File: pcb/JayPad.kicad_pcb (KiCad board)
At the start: 2 copper layers, 113 x 70.8 mm, 51 parts, among them M1 MOUDLE-SEEEDUINO-XIAO, SW1 PEC11-4215F-S24

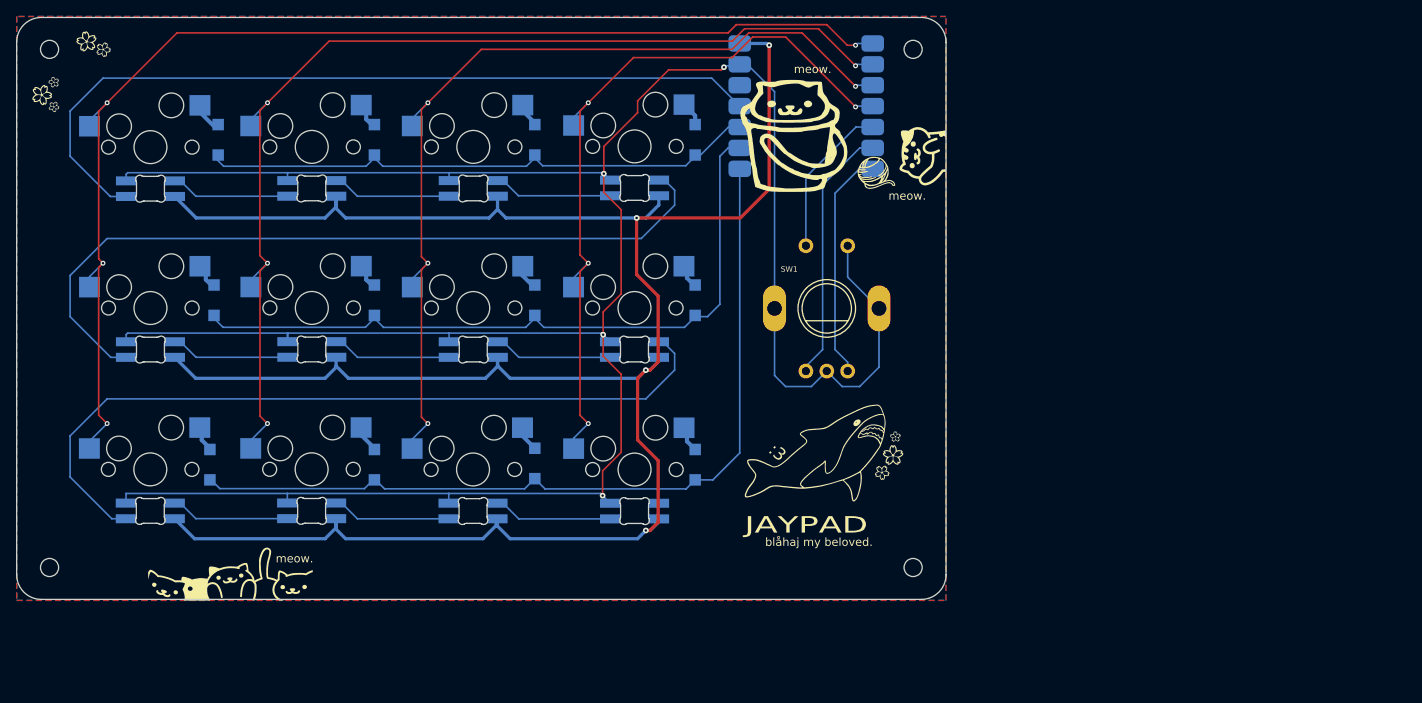
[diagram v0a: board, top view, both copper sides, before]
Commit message: LEDs now using GND copper pour & routed ROW0 which I somehow forgot to do
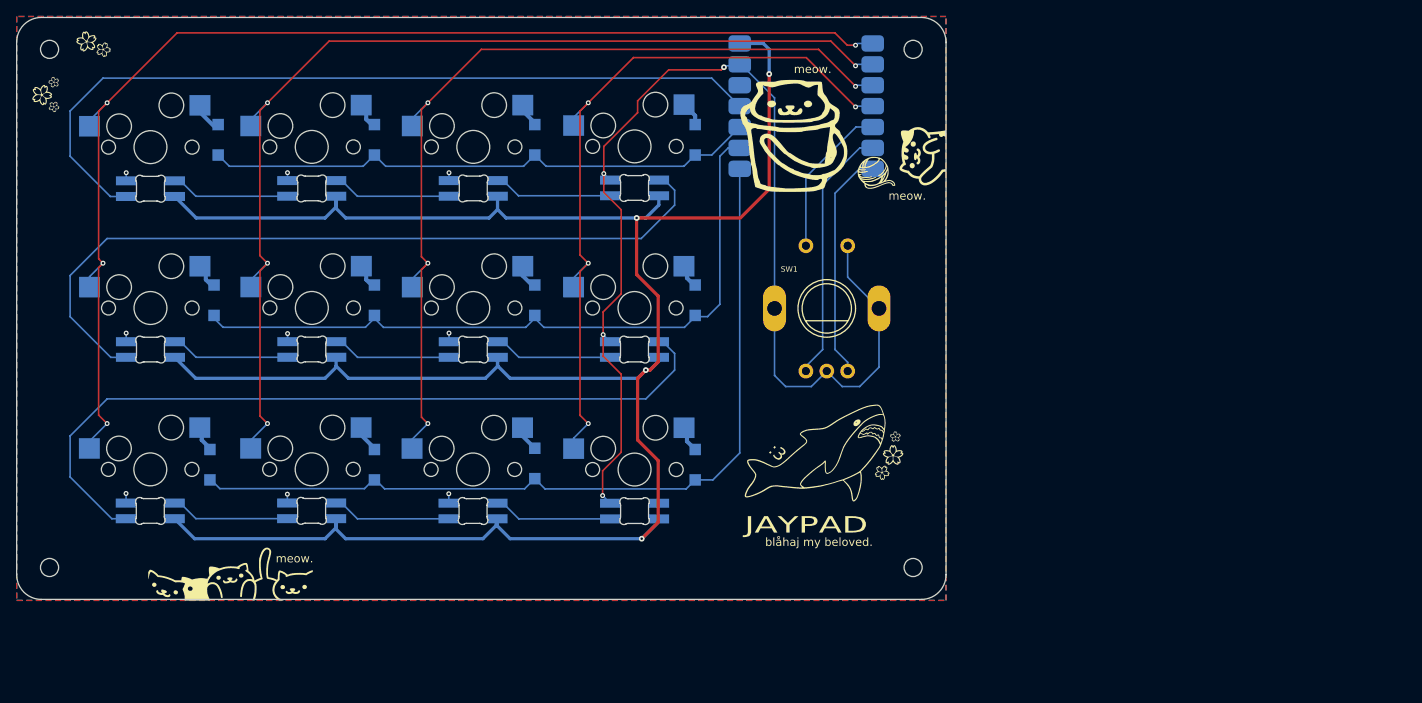
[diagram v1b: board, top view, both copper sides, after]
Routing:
- net GND: track 327.7 -> 152.3 mm, vias 4 -> 13
- net COL3: track 92.9 -> 90.8 mm
- net COL2: track 111.6 -> 109.9 mm
- net COL1: track 130.8 -> 129.5 mm
- net +5V: track 283.9 -> 284.9 mm
- net COL0: track 149.4 -> 148.6 mm

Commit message: Changed from RGB backlight to underglow
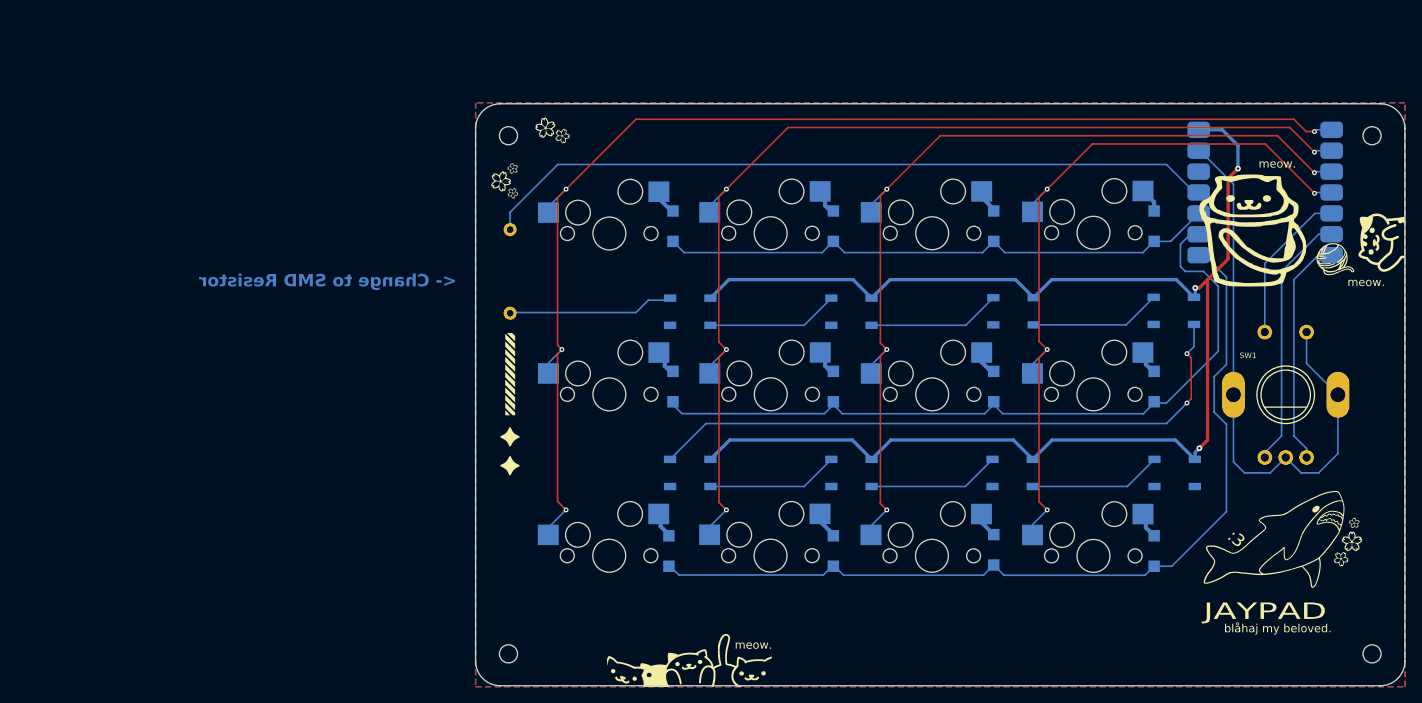
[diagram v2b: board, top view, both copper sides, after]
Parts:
- added G***: LOGO, LOGO, F.Cu at (95.0, 102.5)
- added G***: LOGO, LOGO, F.Cu at (95.0, 91.5)
- added G***: LOGO, LOGO, F.Cu at (95.0, 99.0)
- added LED1: WS2812B, LED_SMD:LED_WS2812B_PLCC4_5.0x5.0mm_P3.2mm, B.Cu at (116.9, 83.9)
- added LED2: WS2812B, LED_SMD:LED_WS2812B_PLCC4_5.0x5.0mm_P3.2mm, B.Cu at (136.5, 83.9)
- added LED3: WS2812B, LED_SMD:LED_WS2812B_PLCC4_5.0x5.0mm_P3.2mm, B.Cu at (156.2, 83.8)
- added LED4: WS2812B, LED_SMD:LED_WS2812B_PLCC4_5.0x5.0mm_P3.2mm, B.Cu at (175.7, 83.8)
- added LED5: WS2812B, LED_SMD:LED_WS2812B_PLCC4_5.0x5.0mm_P3.2mm, B.Cu at (116.9, 103.5)
- added LED6: WS2812B, LED_SMD:LED_WS2812B_PLCC4_5.0x5.0mm_P3.2mm, B.Cu at (136.5, 103.5)
- added LED7: WS2812B, LED_SMD:LED_WS2812B_PLCC4_5.0x5.0mm_P3.2mm, B.Cu at (156.1, 103.5)
- added LED8: WS2812B, LED_SMD:LED_WS2812B_PLCC4_5.0x5.0mm_P3.2mm, B.Cu at (175.8, 103.5)
- added R1: 500, Resistor_THT:R_Axial_DIN0207_L6.3mm_D2.5mm_P10.16mm_Horizontal, B.Cu at (95.0, 73.9)
- S1: renamed from S4; value CherryMX_LTST-A683CEGBW -> CherryMX; footprint JayPad:CherryMX_1.00u_KailhSocket_LTST-A683CEGBW-HS -> JayPad:CherryMX_1.00u_KailhSocket
- S10: renamed from S11; value CherryMX_LTST-A683CEGBW -> CherryMX; footprint JayPad:CherryMX_1.00u_KailhSocket_LTST-A683CEGBW-HS -> JayPad:CherryMX_1.00u_KailhSocket
- S11: renamed from S10; value CherryMX_LTST-A683CEGBW -> CherryMX; footprint JayPad:CherryMX_1.00u_KailhSocket_LTST-A683CEGBW-HS -> JayPad:CherryMX_1.00u_KailhSocket
- S12: renamed from S9; value CherryMX_LTST-A683CEGBW -> CherryMX; footprint JayPad:CherryMX_1.00u_KailhSocket_LTST-A683CEGBW-HS -> JayPad:CherryMX_1.00u_KailhSocket
- S2: renamed from S3; value CherryMX_LTST-A683CEGBW -> CherryMX; footprint JayPad:CherryMX_1.00u_KailhSocket_LTST-A683CEGBW-HS -> JayPad:CherryMX_1.00u_KailhSocket
- S3: renamed from S2; value CherryMX_LTST-A683CEGBW -> CherryMX; footprint JayPad:CherryMX_1.00u_KailhSocket_LTST-A683CEGBW-HS -> JayPad:CherryMX_1.00u_KailhSocket
- S4: renamed from S1; value CherryMX_LTST-A683CEGBW -> CherryMX; footprint JayPad:CherryMX_1.00u_KailhSocket_LTST-A683CEGBW-HS -> JayPad:CherryMX_1.00u_KailhSocket
- S5: renamed from S8; value CherryMX_LTST-A683CEGBW -> CherryMX; footprint JayPad:CherryMX_1.00u_KailhSocket_LTST-A683CEGBW-HS -> JayPad:CherryMX_1.00u_KailhSocket
- S6: renamed from S7; value CherryMX_LTST-A683CEGBW -> CherryMX; footprint JayPad:CherryMX_1.00u_KailhSocket_LTST-A683CEGBW-HS -> JayPad:CherryMX_1.00u_KailhSocket
- S7: renamed from S6; value CherryMX_LTST-A683CEGBW -> CherryMX; footprint JayPad:CherryMX_1.00u_KailhSocket_LTST-A683CEGBW-HS -> JayPad:CherryMX_1.00u_KailhSocket
- S8: renamed from S5; value CherryMX_LTST-A683CEGBW -> CherryMX; footprint JayPad:CherryMX_1.00u_KailhSocket_LTST-A683CEGBW-HS -> JayPad:CherryMX_1.00u_KailhSocket
- S9: renamed from S12; value CherryMX_LTST-A683CEGBW -> CherryMX; footprint JayPad:CherryMX_1.00u_KailhSocket_LTST-A683CEGBW-HS -> JayPad:CherryMX_1.00u_KailhSocket
- moved G*** 57.0 mm to (185.3, 74.0)
- moved :3 56.8 mm to (187.8, 111.5)
- moved D10 56.8 mm to (134.3, 113.0)
- moved D11 56.8 mm to (153.8, 112.8)
- moved D12 56.8 mm to (173.3, 113.0)
- moved D2 56.8 mm to (134.3, 73.5)
- moved D3 56.8 mm to (153.8, 73.5)
- moved D4 56.8 mm to (173.3, 73.5)
- moved D6 56.8 mm to (134.3, 93.0)
- moved D7 56.8 mm to (153.8, 93.0)
- moved D8 56.8 mm to (173.3, 93.0)
- moved G*** 56.8 mm to (195.3, 77.5)
- moved G*** 56.8 mm to (189.6, 116.1)
- moved G*** 56.8 mm to (164.8, 62.0)
- moved G*** 56.8 mm to (197.6, 109.6)
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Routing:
- net +5V: track 284.9 -> 181.6 mm, vias 4 -> 3
- net Net-(S8-DOUT): track 95.3 -> 0.00 mm
- net Net-(S4-DOUT): track 95.2 -> 0.00 mm
- net GND: track 152.3 -> 71.8 mm, vias 13 -> 0
- net DOUT0: track 0.00 -> 76.0 mm, vias 0 -> 2
- net Net-(LED4-DIN): track 0.00 -> 20.2 mm
- net Net-(LED2-DIN): track 0.00 -> 16.2 mm
- net Net-(LED7-DOUT): track 0.00 -> 16.2 mm
- net Net-(LED6-DOUT): track 0.00 -> 16.1 mm
- net Net-(LED5-DOUT): track 0.00 -> 16.1 mm
- net Net-(LED3-DIN): track 0.00 -> 16.1 mm
- net Net-(LED1-DIN): track 0.00 -> 16.0 mm
- net Net-(S11-DOUT): track 14.5 -> 0.00 mm
- net Net-(S2-DOUT): track 14.5 -> 0.00 mm
- net Net-(S6-DOUT): track 14.5 -> 0.00 mm
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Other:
- board text added: "<- Change to SMD Resistor"

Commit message: Added some lil silkscreen decor
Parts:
- added G***: LOGO, LOGO, B.Cu at (180.5, 118.5)
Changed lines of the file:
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@@
+	(footprint "LOGO"
+		(layer "B.Cu")
+		(at 180.5 118.5 -90)
+		(property "Reference" "G***"
+			(at 0 0 90)
+			(layer "B.SilkS")
+			(hide yes)
+			(effects
+				(font
+					(size 1.5 1.5)
+					(thickness 0.3)
+				)
+				(justify mirror)
+			)
+		)
+		(property "Value" "LOGO"
+			(at 0.75 0 90)
+			(layer "B.SilkS")
+			(hide yes)
+			(effects
+				(font
+					(size 1.5 1.5)
+					(thickness 0.3)
+				)
+				(justify mirror)
+			)
+		)
+		(property "Footprint" ""
+			(at 0 0 90)
+			(layer "B.Fab")
+			(hide yes)
+			(effects
+				(font
+					(size 1.27 1.27)
+					(thickness 0.15)
+				)
+				(justify mirror)
+			)
+		)
+		(property "Datasheet" ""
+			(at 0 0 90)
+			(layer "B.Fab")
+			(hide yes)
+			(effects
+				(font
+					(size 1.27 1.27)
+					(thickness 0.15)
+				)
+				(justify mirror)
+			)
+		)
+		(property "Description" ""
+			(at 0 0 90)
+			(layer "B.Fab")
+			(hide yes)
+			(effects
+				(font
+					(size 1.27 1.27)
+					(thickness 0.15)
+				)
+				(justify mirror)
+			)
+		)
+		(attr board_only exclude_from_pos_files exclude_from_bom)
+		(fp_poly
+			(pts
+				(xy -0.980545 0.595625) (xy -0.655868 0.595006) (xy -1.263368 -0.007244) (xy -1.870868 -0.609494)
+				(xy -2.190805 -0.609494) (xy -2.510741 -0.609494) (xy -1.907981 -0.006625) (xy -1.305221 0.596244)
+			)
+			(stroke
+				(width 0)
+				(type solid)
+			)
+			(fill solid)
+			(layer "B.SilkS")
+		)
+		(fp_poly
+			(pts
+				(xy 3.67016 0.595625) (xy 3.994836 0.595006) (xy 3.387336 -0.007244) (xy 2.779836 -0.609494) (xy 2.4599 -0.609494)
+				(xy 2.139963 -0.609494) (xy 2.742723 -0.006625) (xy 3.345483 0.596244)
+			)
+			(stroke
+				(width 0)
+				(type solid)
+			)
+			(fill solid)
+			(layer "B.SilkS")
+		)
+		(fp_poly
+			(pts
+				(xy 5.005381 0.076679) (xy 5.008935 -0.244294) (xy 4.826685 -0.426894) (xy 4.644435 -0.609494) (xy 4.319701 -0.609494)
+				(xy 3.994967 -0.609494) (xy 4.498396 -0.10592) (xy 5.001826 0.397653)
+			)
+			(stroke
+				(width 0)
+				(type solid)
+			)
+			(fill solid)
+			(layer "B.SilkS")
+		)
+		(fp_poly
+			(pts
+				(xy -3.126969 -0.006625) (xy -3.729729 -0.609494) (xy -4.050113 -0.609494) (xy -4.370497 -0.609494)
+				(xy -3.770671 -0.006625) (xy -3.170845 0.596244) (xy -2.847527 0.596244) (xy -2.524209 0.596244)
+			)
+			(stroke
+				(width 0)
+				(type solid)
+			)
+			(fill solid)
+			(layer "B.SilkS")
+		)
+		(fp_poly
+			(pts
+				(xy -0.331246 -0.006625) (xy -0.934006 -0.609494) (xy -1.258628 -0.609494) (xy -1.58325 -0.609494)
+				(xy -0.98049 -0.006625) (xy -0.37773 0.596244) (xy -0.053108 0.596244) (xy 0.271513 0.596244)
+			)
+			(stroke
+				(width 0)
+				(type solid)
+			)
+			(fill solid)
+			(layer "B.SilkS")
+		)
+		(fp_poly
+			(pts
+				(xy 0.596244 -0.006625) (xy -0.006515 -0.609494) (xy -0.331137 -0.609494) (xy -0.655759 -0.609494)
+				(xy -0.052999 -0.006625) (xy 0.549761 0.596244) (xy 0.874383 0.596244) (xy 1.199004 0.596244)
+			)
+			(stroke
+				(width 0)
+				(type solid)
+			)
+			(fill solid)
+			(layer "B.SilkS")
+		)
+		(fp_poly
+			(pts
+				(xy 1.523735 -0.006625) (xy 0.920975 -0.609494) (xy 0.600419 -0.609494) (xy 0.279862 -0.609494)
+				(xy 0.879312 -0.006625) (xy 1.478762 0.596244) (xy 1.802628 0.596244) (xy 2.126495 0.596244)
+			)
+			(stroke
+				(width 0)
+				(type solid)
+			)
+			(fill solid)
+			(layer "B.SilkS")
+		)
+		(fp_poly
+			(pts
+				(xy 4.319458 -0.006625) (xy 3.716698 -0.609494) (xy 3.392076 -0.609494) (xy 3.067454 -0.609494)
+				(xy 3.670214 -0.006625) (xy 4.272974 0.596244) (xy 4.597596 0.596244) (xy 4.922218 0.596244)
+			)
+			(stroke
+				(width 0)
+				(type solid)
+			)
+			(fill solid)
+			(layer "B.SilkS")
+		)
+		(fp_poly
+			(pts
+				(xy -4.05446 -0.006625) (xy -4.65722 -0.609494) (xy -4.82621 -0.609494) (xy -4.9952 -0.609494) (xy -4.9952 -0.453735)
+				(xy -4.9952 -0.297976) (xy -4.547945 0.149134) (xy -4.10069 0.596244) (xy -3.776195 0.596244) (xy -3.4517 0.596244)
+			)
+			(stroke
+				(width 0)
+				(type solid)
+			)
+			(fill solid)
+			(layer "B.SilkS")
+		)
+		(fp_poly
+			(pts
+				(xy 5.008451 -0.567265) (xy 5.005636 -0.596567) (xy 4.991975 -0.607852) (xy 4.968701 -0.609494)
+				(xy 4.940765 -0.60829) (xy 4.928954 -0.605391) (xy 4.928952 -0.605348) (xy 4.937565 -0.594526) (xy 4.959142 -0.5724)
+				(xy 4.968701 -0.563119) (xy 5.008451 -0.525037)
+			)
+			(stroke
+				(width 0)
+				(type solid)
+			)
+			(fill solid)
+			(layer "B.SilkS")
+		)
+		(fp_poly
+			(pts
+				(xy -1.996358 0.191664) (xy -2.090145 0.096023) (xy -2.186794 -0.001878) (xy -2.282844 -0.098577)
+				(xy -2.374831 -0.190611) (xy -2.459293 -0.274518) (xy -2.532767 -0.346834) (xy -2.59179 -0.404098)
+				(xy -2.599215 -0.411205) (xy -2.806828 -0.609494) (xy -3.127014 -0.609494) (xy -3.4472 -0.609494)
+				(xy -2.839902 -0.007225) (xy -2.232603 0.595044) (xy -1.916858 0.595644) (xy -1.601114 0.596244)
+			)
+			(stroke
+				(width 0)
+				(type solid)
+			)
+			(fill solid)
+			(layer "B.SilkS")
+		)
+		(fp_poly
+			(pts
+				(xy 2.63596 0.173998) (xy 2.541453 0.077824) (xy 2.445271 -0.019502) (xy 2.350576 -0.114815) (xy 2.260532 -0.204953)
+				(xy 2.178303 -0.286751) (xy 2.107053 -0.357046) (xy 2.049946 -0.412674) (xy 2.03307 -0.428871) (xy 1.843806 -0.609494)
+				(xy 1.523655 -0.609494) (xy 1.203504 -0.609494) (xy 1.810803 -0.007225) (xy 2.418102 0.595044) (xy 2.733843 0.595644)
+				(xy 3.049585 0.596244)
+			)
+			(stroke
+				(width 0)
+				(type solid)
+			)
+			(fill solid)
+			(layer "B.SilkS")
+		)
+		(fp_poly
+			(pts
+				(xy -4.683829 0.291497) (xy -4.757367 0.218008) (xy -4.824721 0.150894) (xy -4.883661 0.09236) (xy -4.931962 0.044611)
+				(xy -4.967394 0.009851) (xy -4.987729 -0.009716) (xy -4.99178 -0.01325) (xy -4.992753 -0.000616)
+				(xy -4.993618 0.034818) (xy -4.994334 0.089354) (xy -4.99486 0.159294) (xy -4.995153 0.240937) (xy -4.9952 0.291497)
+				(xy -4.9952 0.596244) (xy -4.687249 0.596244) (xy -4.379298 0.596244)
+			)
+			(stroke
+				(width 0)
+				(type solid)
+			)
+			(fill solid)
+			(layer "B.SilkS")
+		)
+	)
 	(footprint "LOGO"
 		(layer "B.Cu")

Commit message: Added a bit more decor and changed resistor placement
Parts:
- added G***: LOGO, LOGO, B.Cu at (178.0, 122.0)
- R1: moved to F.Cu
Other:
- board text removed: "<- Change to SMD Resistor"
